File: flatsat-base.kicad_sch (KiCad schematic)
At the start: 21 parts, among them J1 FFC2B28-24-G, J10 Conn_01x24_Male, J11 Conn_01x10_Male, J12 FFC2B28-10-G, J13 FFC2B28-10-G, J14 Screw_Terminal_01x02, J15 Screw_Terminal_01x02, J2 FFC2B28-10-G, J3 FFC2B28-10-G, J4 FFC2B28-10-G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

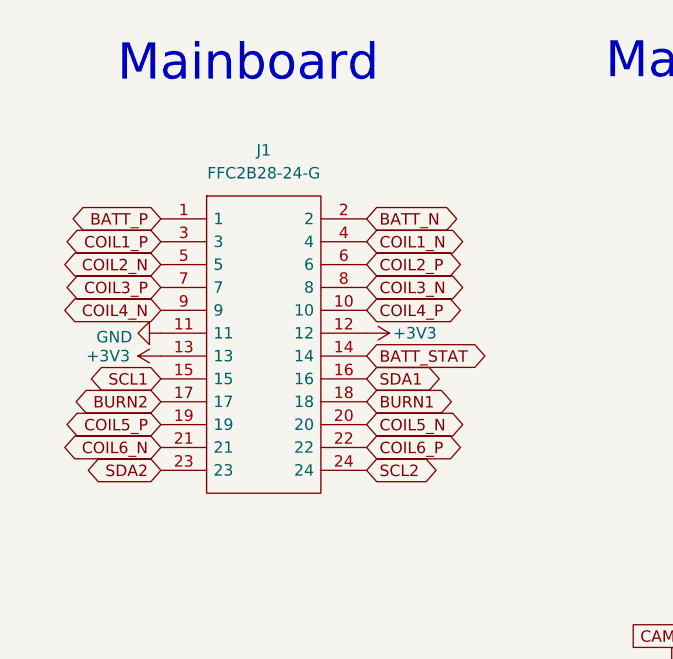
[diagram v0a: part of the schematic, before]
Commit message: Attachment points for BATT_P/BATT_N and routed
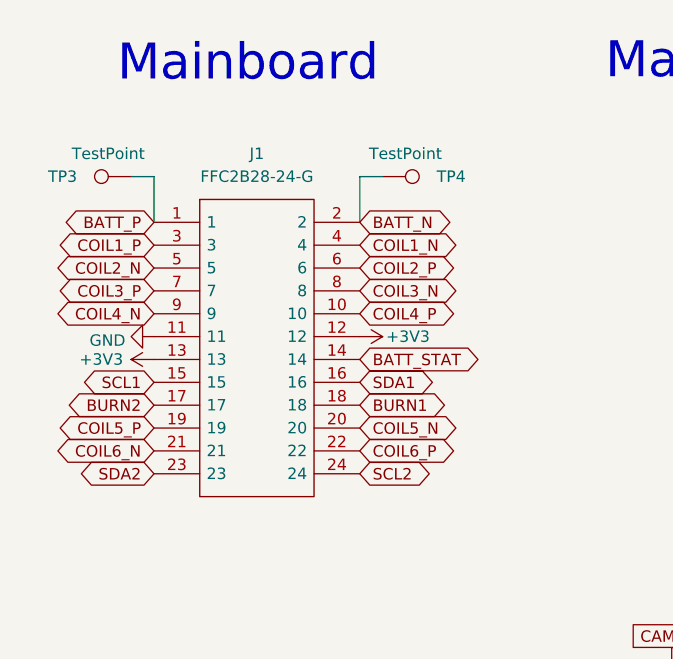
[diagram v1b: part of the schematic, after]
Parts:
- added TP3, TP4: TestPoint, TestPoint:TestPoint_Plated_Hole_D5.0mm, symbol Connector:TestPoint
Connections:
- net BATT_N: now also TP4.1
- net BATT_P: now also TP3.1
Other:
- moved on the sheet: J1

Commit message: misc changes
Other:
- note added: "flatsat v01"
- moved on the sheet: H1, H2, H3, H4, J1, J10, J11, J12, J13, J14, J15, J2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
